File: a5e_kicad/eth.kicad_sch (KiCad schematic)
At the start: 35 parts, among them U1501 KSZ9031RNXCA

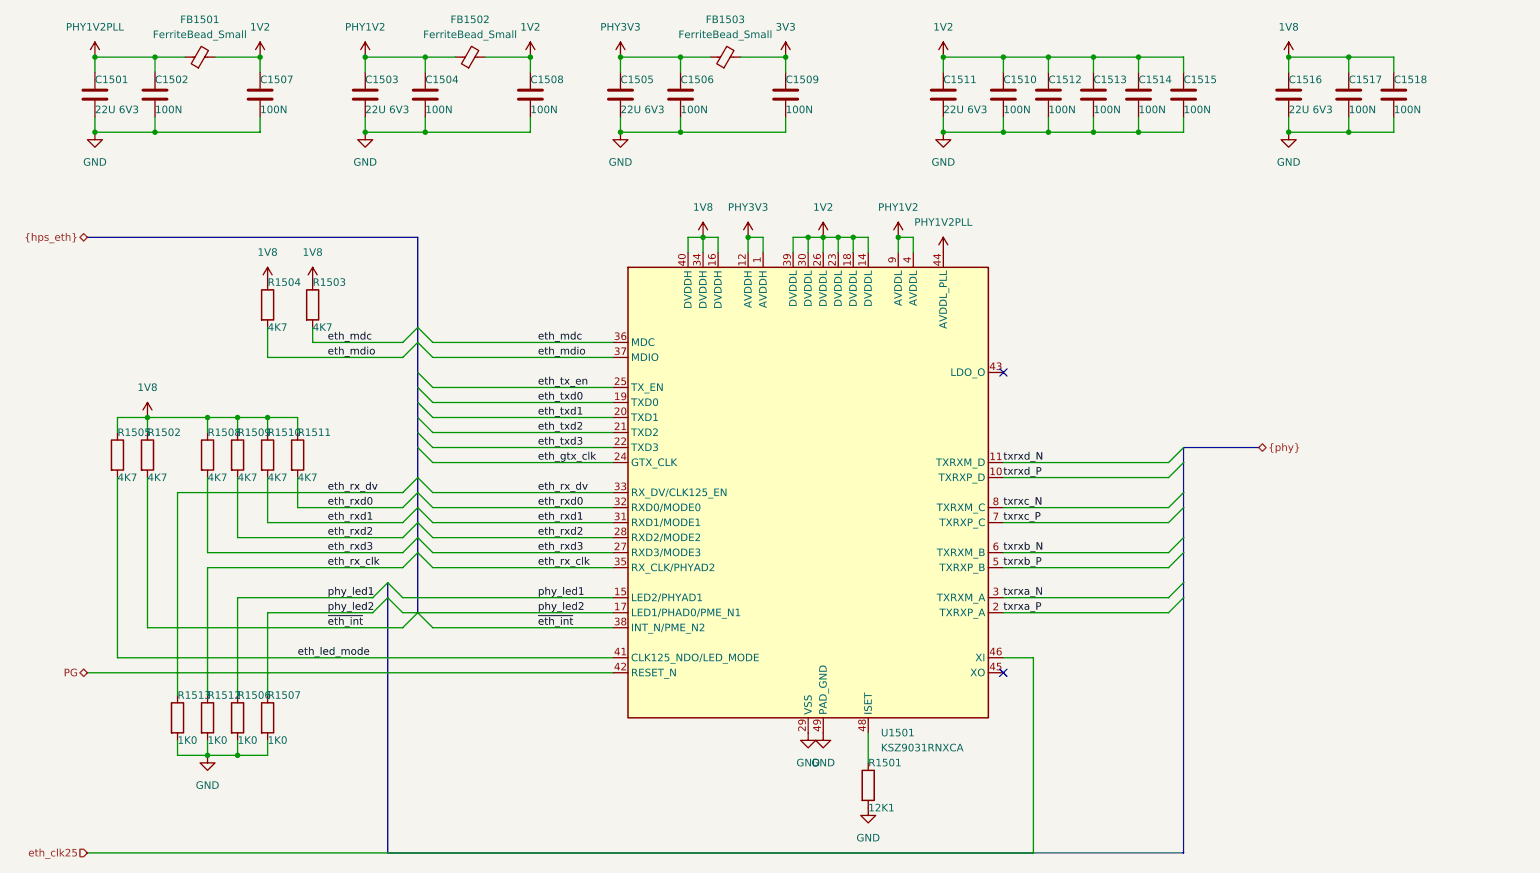
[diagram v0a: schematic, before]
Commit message: add vias to lppdr balls
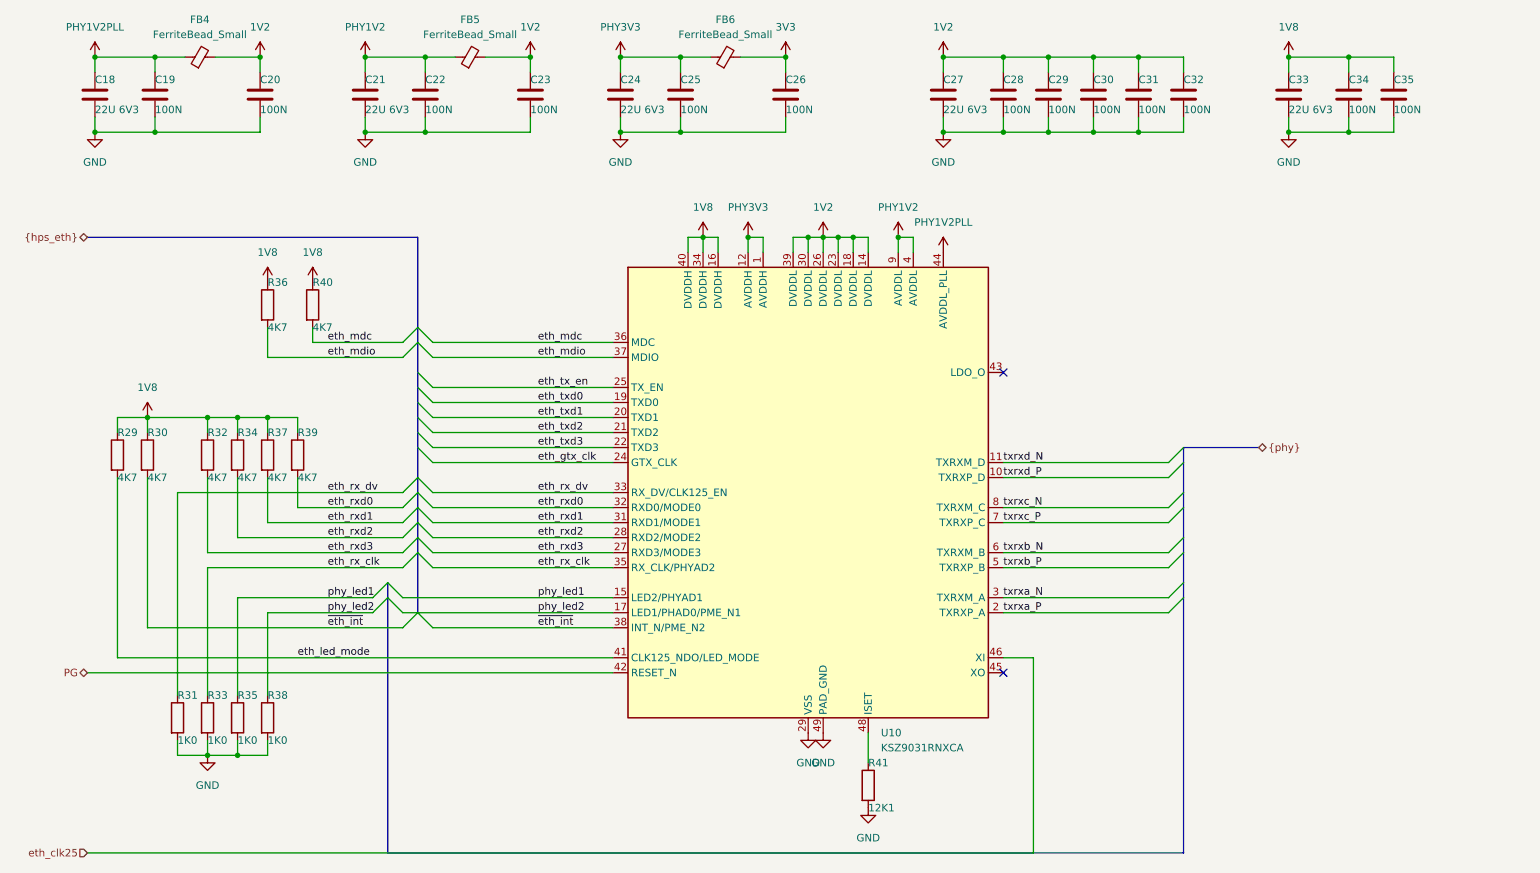
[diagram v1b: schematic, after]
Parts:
- renumbered C1501 to C18, C1502 to C19, C1507 to C20, C1503 to C21, C1504 to C22, C1508 to C23, C1505 to C24, C1506 to C25, C1509 to C26, C1511 to C27, C1510 to C28, C1512 to C29, C1513 to C30, C1514 to C31, C1515 to C32, C1516 to C33, C1517 to C34, C1518 to C35, FB1501 to FB4, FB1502 to FB5, FB1503 to FB6, R1505 to R29, R1502 to R30, R1513 to R31, R1508 to R32, R1512 to R33, R1509 to R34, R1506 to R35, R1504 to R36, R1510 to R37, R1507 to R38, R1511 to R39, R1503 to R40, R1501 to R41, U1501 to U10

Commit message: add comments
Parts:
- added J9: RJ45_RB1-125B8G1A, Connector_RJ:RJ45_UDE_RB1-125B8G1A, symbol Connector:RJ45_RB1-125B8G1A
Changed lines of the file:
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@@
 	)
 	(bus_entry
-		(at 220.98 106.68)
+		(at 209.55 106.68)
 		(size -2.54 2.54)
 		(stroke
@@
 	)
 	(bus_entry
-		(at 220.98 104.14)
+		(at 209.55 104.14)
 		(size -2.54 2.54)
 		(stroke
@@
 	)
 	(bus_entry
-		(at 220.98 99.06)
+		(at 209.55 99.06)
 		(size -2.54 2.54)
 		(stroke
@@
 	)
 	(bus_entry
-		(at 220.98 114.3)
+		(at 209.55 114.3)
 		(size -2.54 2.54)
 		(stroke
@@
 	)
 	(bus_entry
-		(at 220.98 111.76)
+		(at 209.55 111.76)
 		(size -2.54 2.54)
 		(stroke
@@
 	)
 	(bus_entry
-		(at 220.98 96.52)
+		(at 209.55 96.52)
 		(size -2.54 2.54)
 		(stroke
@@
 	)
 	(bus_entry
-		(at 220.98 88.9)
+		(at 209.55 88.9)
 		(size -2.54 2.54)
 		(stroke
@@
 	)
 	(bus_entry
-		(at 220.98 91.44)
+		(at 209.55 91.44)
 		(size -2.54 2.54)
 		(stroke
@@
 	(wire
 		(pts
-			(xy 190.5 106.68) (xy 218.44 106.68)
+			(xy 190.5 106.68) (xy 207.01 106.68)
 		)
 		(stroke
@@
 	(bus
 		(pts
-			(xy 220.98 111.76) (xy 220.98 114.3)
+			(xy 209.55 111.76) (xy 209.55 114.3)
 		)
 		(stroke
@@
 	(wire
 		(pts
-			(xy 190.5 93.98) (xy 218.44 93.98)
+			(xy 190.5 93.98) (xy 207.01 93.98)
 		)
 		(stroke
@@
 	(bus
 		(pts
-			(xy 220.98 91.44) (xy 220.98 96.52)
+			(xy 209.55 91.44) (xy 209.55 96.52)
 		)
 		(stroke
@@
 	(bus
 		(pts
-			(xy 220.98 106.68) (xy 220.98 111.76)
+			(xy 209.55 106.68) (xy 209.55 111.76)
 		)
 		(stroke
@@
 	(wire
 		(pts
-			(xy 190.5 91.44) (xy 218.44 91.44)
+			(xy 190.5 91.44) (xy 207.01 91.44)
 		)
 		(stroke
@@
 	(wire
 		(pts
-			(xy 190.5 116.84) (xy 218.44 116.84)
+			(xy 190.5 116.84) (xy 207.01 116.84)
 		)
 		(stroke
@@
 	(wire
 		(pts
-			(xy 190.5 99.06) (xy 218.44 99.06)
+			(xy 190.5 99.06) (xy 207.01 99.06)
 		)
 		(stroke
@@
 	(bus
 		(pts
-			(xy 220.98 88.9) (xy 220.98 91.44)
+			(xy 209.55 54.61) (xy 209.55 91.44)
 		)
 		(stroke
@@
 	(bus
 		(pts
-			(xy 220.98 96.52) (xy 220.98 99.06)
+			(xy 209.55 96.52) (xy 209.55 99.06)
 		)
 		(stroke
@@
 	(bus
 		(pts
-			(xy 86.36 157.48) (xy 220.98 157.48)
+			(xy 86.36 157.48) (xy 209.55 157.48)
 		)
 		(stroke
@@
 	(wire
 		(pts
-			(xy 190.5 109.22) (xy 218.44 109.22)
+			(xy 190.5 109.22) (xy 207.01 109.22)
 		)
 		(stroke
@@
 	(wire
 		(pts
-			(xy 190.5 101.6) (xy 218.44 101.6)
+			(xy 190.5 101.6) (xy 207.01 101.6)
 		)
 		(stroke
@@
 	(bus
 		(pts
-			(xy 220.98 99.06) (xy 220.98 104.14)
+			(xy 209.55 99.06) (xy 209.55 104.14)
 		)
 		(stroke
@@
 	(bus
 		(pts
-			(xy 220.98 88.9) (xy 233.68 88.9)
+			(xy 209.55 54.61) (xy 220.98 54.61)
 		)
 		(stroke
@@
 	(wire
 		(pts
-			(xy 190.5 114.3) (xy 218.44 114.3)
+			(xy 190.5 114.3) (xy 207.01 114.3)
 		)
 		(stroke
@@
 	(bus
 		(pts
-			(xy 220.98 114.3) (xy 220.98 157.48)
+			(xy 209.55 114.3) (xy 209.55 157.48)
 		)
 		(stroke
@@
 	(bus
 		(pts
-			(xy 220.98 104.14) (xy 220.98 106.68)
+			(xy 209.55 104.14) (xy 209.55 106.68)
 		)
 		(stroke
@@
 	(hierarchical_label "{phy}"
 		(shape bidirectional)
-		(at 233.68 88.9 0)
+		(at 220.98 54.61 0)
 		(effects
 			(font
@@
 					(unit 1)
 				)
+			)
+		)
+	)
+	(symbol
+		(lib_id "Connector:RJ45_RB1-125B8G1A")
+		(at 247.65 93.98 180)
+		(unit 1)
+		(body_style 1)
+		(exclude_from_sim no)
+		(in_bom yes)
+		(on_board yes)
+		(in_pos_files yes)
+		(dnp no)
+		(fields_autoplaced yes)
+		(property "Reference" "J9"
+			(at 256.54 93.9799 0)
+			(show_name no)
+			(do_not_autoplace no)
+			(effects
+				(font
+					(size 1.27 1.27)
+				)
+				(justify right)
+			)
+		)
+		(property "Value" "RJ45_RB1-125B8G1A"
+			(at 256.54 96.5199 0)
+			(show_name no)
+			(do_not_autoplace no)
+			(effects
+				(font
+					(size 1.27 1.27)
+				)
+				(justify right)
+			)
+		)
+		(property "Footprint" "Connector_RJ:RJ45_UDE_RB1-125B8G1A"
+			(at 246.38 96.52 0)
+			(hide yes)
+			(show_name no)
+			(do_not_autoplace no)
+			(effects
+				(font
+					(size 1.27 1.27)
+				)
+			)
+		)
+		(property "Datasheet" "https://datasheet.lcsc.com/szlcsc/1901091107_UDE-Corp-RB1-125B8G1A_C363353.pdf"
+			(at 253.746 95.123 0)
+			(hide yes)
+			(show_name no)
+			(do_not_autoplace no)
+			(effects
+				(font
+					(size 1.27 1.27)
+				)
+				(justify left top)
+			)
+		)
+		(property "Description" "LAN Transformer Jack, RJ45, 10/100/1000 BaseT"
+			(at 247.65 93.98 0)
+			(hide yes)
+			(show_name no)
+			(do_not_autoplace no)
+			(effects
+				(font
+					(size 1.27 1.27)
+				)
+			)
+		)
+		(pin "R10"
+		)
+		(pin "L2"
+		)
+		(pin "L4"
+		)
+		(pin "L1"
+		)
+		(pin "L3"
+		)
+		(pin "R2"
+		)
+		(pin "R6"
+		)
+		(pin "R8"
+		)
+		(pin "R1"
+		)
+		(pin "R5"
+		)
+		(pin "SH"
+		)
+		(pin "R9"
+		)
+		(pin "R3"
+		)
+		(pin "R7"
+		)
+		(pin "R4"
+		)
+		(instances
+			(project "agilex_3_soc"
+				(path "/a5b98d95-6877-4284-904f-d04e32723ae0/cf2987d8-8050-440f-9afe-54dd4a6786f5"
+					(reference "J9")
+					(unit 1)
+				)

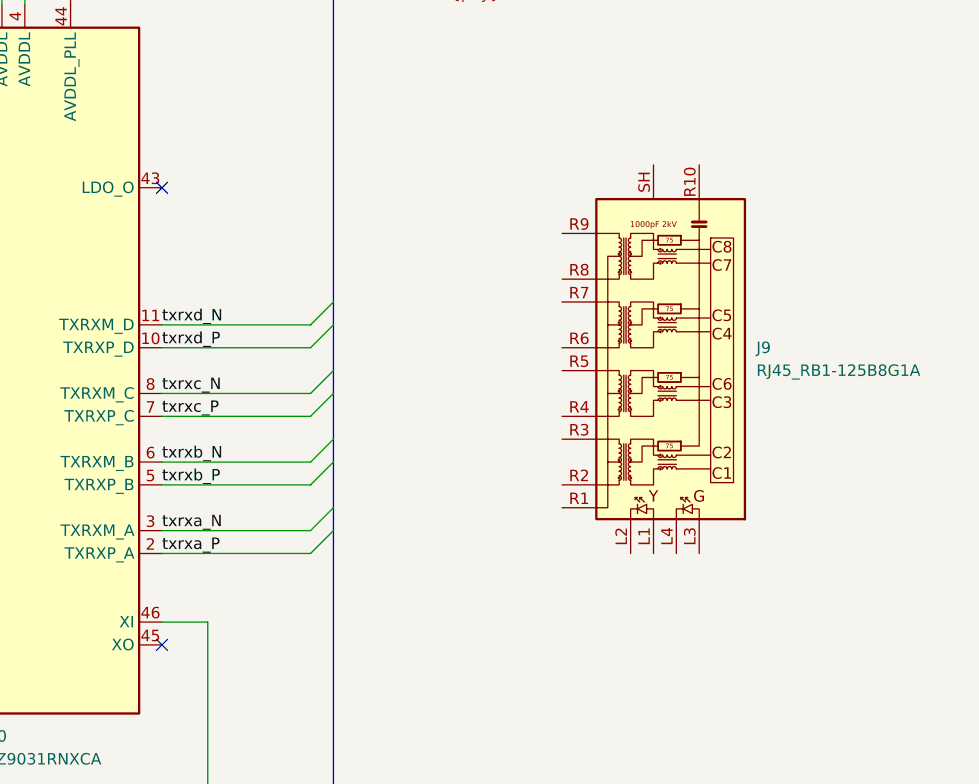
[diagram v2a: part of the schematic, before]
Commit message: route ethernet rgmii io
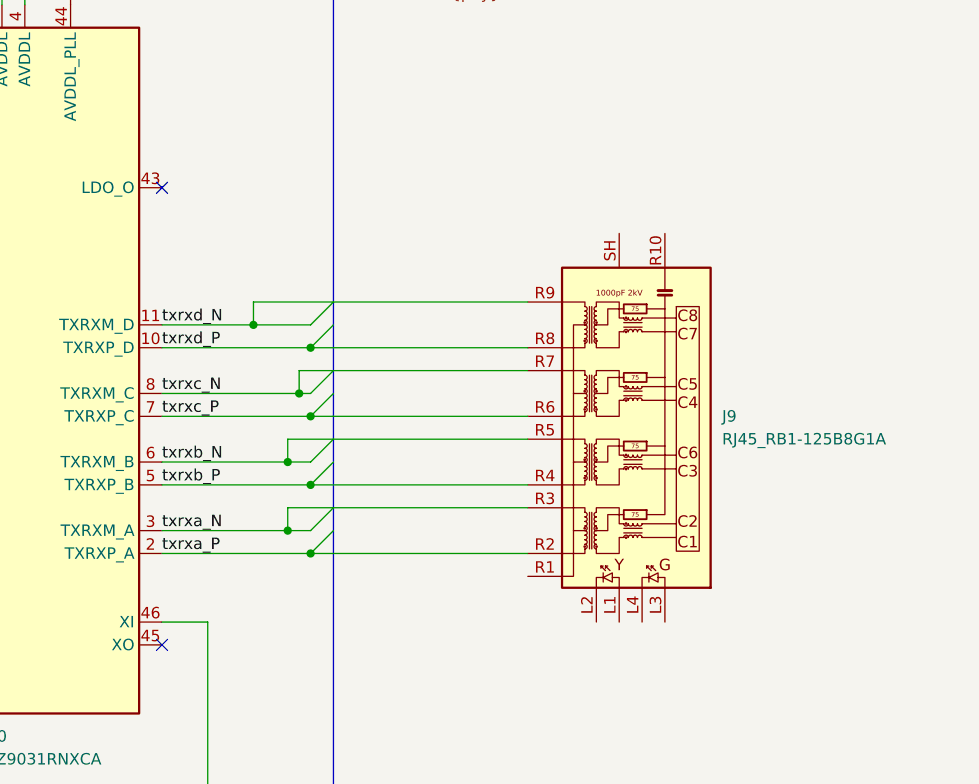
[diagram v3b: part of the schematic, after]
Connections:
- net txrxa_N: now also J9.R3 (TD1-)
- net txrxa_P: now also J9.R2 (TD1+)
- net txrxb_N: now also J9.R5 (TD2-)
- net txrxb_P: now also J9.R4 (TD2+)
- net txrxc_N: now also J9.R7 (TD3-)
- net txrxc_P: now also J9.R6 (TD3+)
- net txrxd_N: now also J9.R9 (TD4-)
- net txrxd_P: now also J9.R8 (TD4+)
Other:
- moved on the sheet: J9
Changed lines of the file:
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@@
 	)
 	(junction
+		(at 205.74 99.06)
+		(diameter 0)
+		(color 0 0 0 0)
+	)
+	(junction
 		(at 92.71 35.56)
 		(diameter 0)
@@
 	)
 	(junction
+		(at 204.47 114.3)
+		(diameter 0)
+		(color 0 0 0 0)
+	)
+	(junction
 		(at 147.32 53.34)
 		(diameter 0)
@@
 	)
 	(junction
+		(at 200.66 91.44)
+		(diameter 0)
+		(color 0 0 0 0)
+	)
+	(junction
 		(at 180.34 35.56)
 		(diameter 0)
@@
 	)
 	(junction
+		(at 207.01 101.6)
+		(diameter 0)
+		(color 0 0 0 0)
+	)
+	(junction
 		(at 157.48 53.34)
 		(diameter 0)
@@
 	)
 	(junction
+		(at 204.47 106.68)
+		(diameter 0)
+		(color 0 0 0 0)
+	)
+	(junction
 		(at 190.5 22.86)
 		(diameter 0)
@@
 	)
 	(junction
+		(at 207.01 109.22)
+		(diameter 0)
+		(color 0 0 0 0)
+	)
+	(junction
+		(at 207.01 93.98)
+		(diameter 0)
+		(color 0 0 0 0)
+	)
+	(junction
 		(at 92.71 22.86)
 		(diameter 0)
@@
 	)
 	(junction
+		(at 207.01 116.84)
+		(diameter 0)
+		(color 0 0 0 0)
+	)
+	(junction
 		(at 82.55 35.56)
 		(diameter 0)
@@
 	(wire
 		(pts
+			(xy 205.74 99.06) (xy 205.74 96.52)
+		)
+		(stroke
+			(width 0)
+			(type default)
+		)
+	)
+	(wire
+		(pts
 			(xy 160.02 53.34) (xy 162.56 53.34)
 		)
@@
 	(wire
 		(pts
+			(xy 200.66 91.44) (xy 200.66 88.9)
+		)
+		(stroke
+			(width 0)
+			(type default)
+		)
+	)
+	(wire
+		(pts
 			(xy 46.99 22.86) (xy 52.07 22.86)
 		)
@@
 	(wire
 		(pts
+			(xy 200.66 91.44) (xy 207.01 91.44)
+		)
+		(stroke
+			(width 0)
+			(type default)
+		)
+	)
+	(wire
+		(pts
 			(xy 149.86 55.88) (xy 149.86 53.34)
 		)
@@
 	(wire
 		(pts
+			(xy 204.47 114.3) (xy 204.47 111.76)
+		)
+		(stroke
+			(width 0)
+			(type default)
+		)
+	)
+	(wire
+		(pts
 			(xy 71.12 93.98) (xy 71.12 99.06)
 		)
@@
 	(wire
 		(pts
-			(xy 190.5 106.68) (xy 207.01 106.68)
+			(xy 190.5 106.68) (xy 204.47 106.68)
 		)
 		(stroke
@@
 	(wire
 		(pts
+			(xy 207.01 93.98) (xy 231.14 93.98)
+		)
+		(stroke
+			(width 0)
+			(type default)
+		)
+	)
+	(wire
+		(pts
 			(xy 88.9 116.84) (xy 91.44 116.84)
 		)
@@
 	(wire
 		(pts
-			(xy 190.5 91.44) (xy 207.01 91.44)
+			(xy 190.5 91.44) (xy 200.66 91.44)
 		)
 		(stroke
@@
 	(wire
 		(pts
-			(xy 190.5 99.06) (xy 207.01 99.06)
+			(xy 190.5 99.06) (xy 205.74 99.06)
 		)
 		(stroke
@@
 	(wire
 		(pts
+			(xy 205.74 99.06) (xy 207.01 99.06)
+		)
+		(stroke
+			(width 0)
+			(type default)
+		)
+	)
+	(wire
+		(pts
 			(xy 180.34 22.86) (xy 180.34 25.4)
 		)
@@
 	(wire
 		(pts
+			(xy 204.47 106.68) (xy 204.47 104.14)
+		)
+		(stroke
+			(width 0)
+			(type default)
+		)
+	)
+	(wire
+		(pts
 			(xy 92.71 22.86) (xy 97.79 22.86)
 		)
@@
 	(wire
 		(pts
+			(xy 207.01 101.6) (xy 231.14 101.6)
+		)
+		(stroke
+			(width 0)
+			(type default)
+		)
+	)
+	(wire
+		(pts
 			(xy 50.8 96.52) (xy 88.9 96.52)
 		)
@@
 	(wire
 		(pts
+			(xy 200.66 88.9) (xy 231.14 88.9)
+		)
+		(stroke
+			(width 0)
+			(type default)
+		)
+	)
+	(wire
+		(pts
 			(xy 198.12 35.56) (xy 205.74 35.56)
 		)
@@
 	(wire
 		(pts
+			(xy 207.01 109.22) (xy 231.14 109.22)
+		)
+		(stroke
+			(width 0)
+			(type default)
+		)
+	)
+	(wire
+		(pts
+			(xy 204.47 111.76) (xy 231.14 111.76)
+		)
+		(stroke
+			(width 0)
+			(type default)
+		)
+	)
+	(wire
+		(pts
 			(xy 66.04 138.43) (xy 66.04 140.97)
 		)
@@
 		)
 	)
+	(wire
+		(pts
+			(xy 207.01 116.84) (xy 231.14 116.84)
+		)
+		(stroke
+			(width 0)
+			(type default)
+		)
+	)
 	(bus
 		(pts
@@
 	(wire
 		(pts
-			(xy 190.5 114.3) (xy 207.01 114.3)
+			(xy 190.5 114.3) (xy 204.47 114.3)
+		)
+		(stroke
+			(width 0)
+			(type default)
+		)
+	)
+	(wire
+		(pts
+			(xy 204.47 114.3) (xy 207.01 114.3)
 		)
 		(stroke
@@
 	(wire
 		(pts
+			(xy 204.47 106.68) (xy 207.01 106.68)
+		)
+		(stroke
+			(width 0)
+			(type default)
+		)
+	)
+	(wire
+		(pts
 			(xy 66.04 93.98) (xy 66.04 101.6)
 		)
@@
 	(wire
 		(pts
+			(xy 204.47 104.14) (xy 231.14 104.14)
+		)
+		(stroke
+			(width 0)
+			(type default)
+		)
+	)
+	(wire
+		(pts
 			(xy 55.88 106.68) (xy 88.9 106.68)
 		)
@@
 	(wire
 		(pts
+			(xy 205.74 96.52) (xy 231.14 96.52)
+		)
+		(stroke
+			(width 0)
+			(type default)
+		)
+	)
+	(wire
+		(pts
 			(xy 55.88 83.82) (xy 55.88 86.36)
 		)
@@
 	(symbol
 		(lib_id "Connector:RJ45_RB1-125B8G1A")
-		(at 247.65 93.98 180)
+		(at 243.84 101.6 180)
 		(unit 1)
 		(body_style 1)
@@
 		(in_pos_files yes)
 		(dnp no)
-		(fields_autoplaced yes)
 		(property "Reference" "J9"
-			(at 256.54 93.9799 0)
+			(at 252.73 101.5999 0)
 			(show_name no)
 			(do_not_autoplace no)
@@
 		)
 		(property "Value" "RJ45_RB1-125B8G1A"
-			(at 256.54 96.5199 0)
+			(at 252.73 104.1399 0)
 			(show_name no)
 			(do_not_autoplace no)
@@
 		)
 		(property "Footprint" "Connector_RJ:RJ45_UDE_RB1-125B8G1A"
-			(at 246.38 96.52 0)
+			(at 242.57 104.14 0)
 			(hide yes)
 			(show_name no)
@@
 		)
 		(property "Datasheet" "https://datasheet.lcsc.com/szlcsc/1901091107_UDE-Corp-RB1-125B8G1A_C363353.pdf"
-			(at 253.746 95.123 0)
+			(at 249.936 102.743 0)
 			(hide yes)
 			(show_name no)
@@
 		)
 		(property "Description" "LAN Transformer Jack, RJ45, 10/100/1000 BaseT"
-			(at 247.65 93.98 0)
+			(at 243.84 101.6 0)
 			(hide yes)
 			(show_name no)

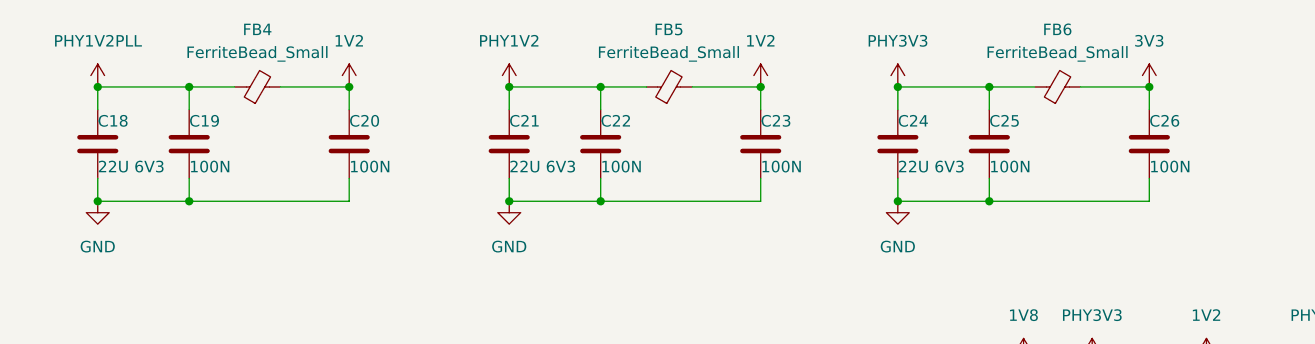
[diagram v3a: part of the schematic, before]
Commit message: remove hyperram and add lpddr4 bypass caps
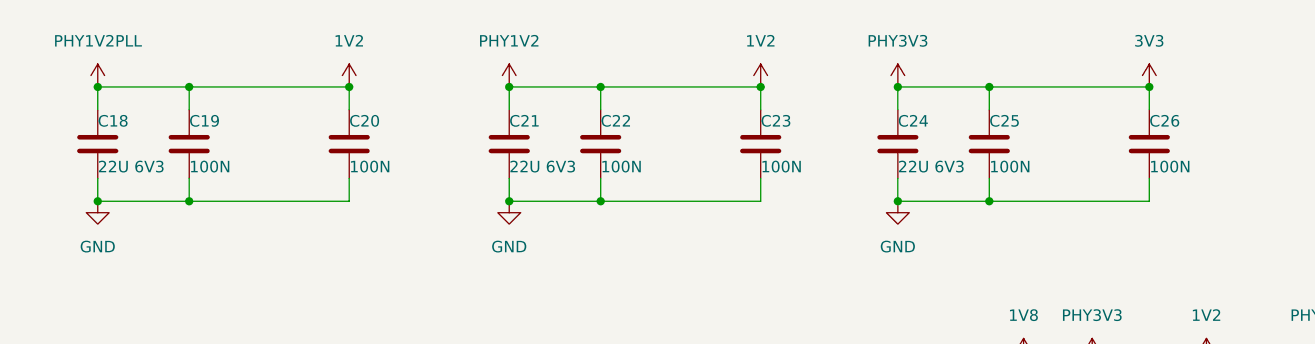
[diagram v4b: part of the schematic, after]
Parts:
- removed FB4, FB5, FB6: FerriteBead_Small, Capacitor_SMD:C_0603_1608Metric, symbol Device:FerriteBead_Small
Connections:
- net PHY1V2 is gone; now on net 1V2: C21.1, C22.1, U10.4 (AVDDL), U10.9 (AVDDL)
- net PHY1V2PLL is gone; now on net 1V2: C18.1, C19.1, U10.44 (AVDDL_PLL)
- net PHY3V3 is gone; now on net 3V3: C24.1, C25.1, U10.1 (AVDDH), U10.12 (AVDDH)

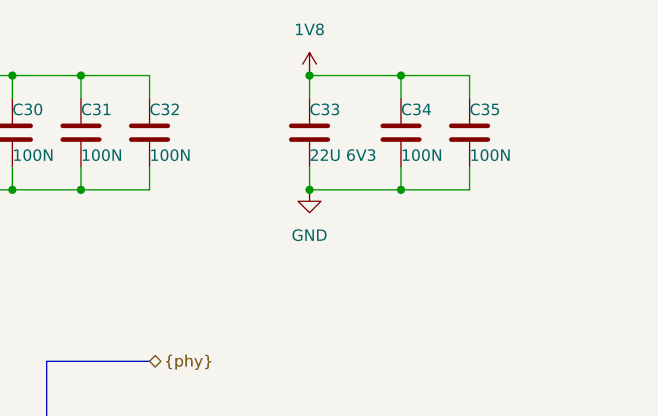
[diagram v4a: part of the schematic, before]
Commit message: remove extra components and make 1v8 plane
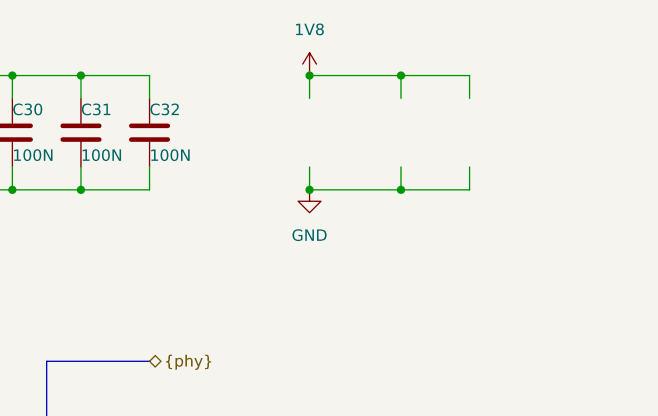
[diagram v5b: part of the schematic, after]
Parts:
- removed C33: 22U 6V3, Capacitor_SMD:C_0402_1005Metric, symbol Device:C
- removed C34, C35: 100N, Capacitor_SMD:C_0402_1005Metric, symbol Device:C
